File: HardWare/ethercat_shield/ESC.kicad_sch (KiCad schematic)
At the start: 39 parts, among them U8 AX58100-LQPF80, U9 BL24C16F-PARC, X1 25M

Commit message: Add test version
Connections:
- net GNDA is gone; now on net GND: C39.2, C40.2, C41.2, C42.2, C49.2
- net GNDD is gone; now on net GND: C35.2, C36.2, C37.2, C38.2, C43.2, C44.2, C45.2, C46.2, C47.2, C48.2

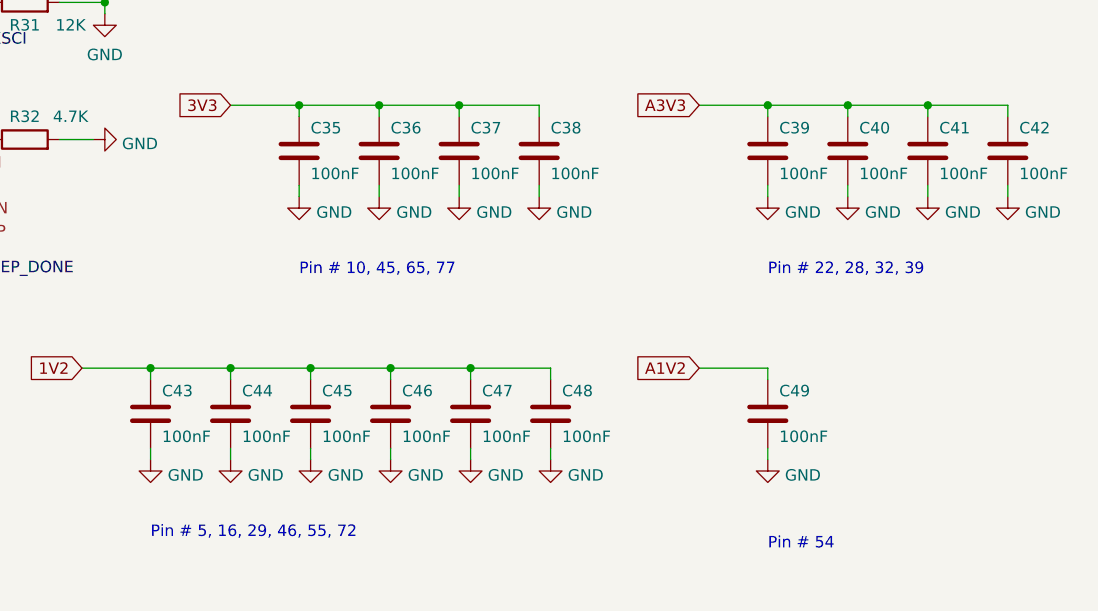
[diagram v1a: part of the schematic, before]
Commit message: 'ethercat_shield' PCB_layout completed
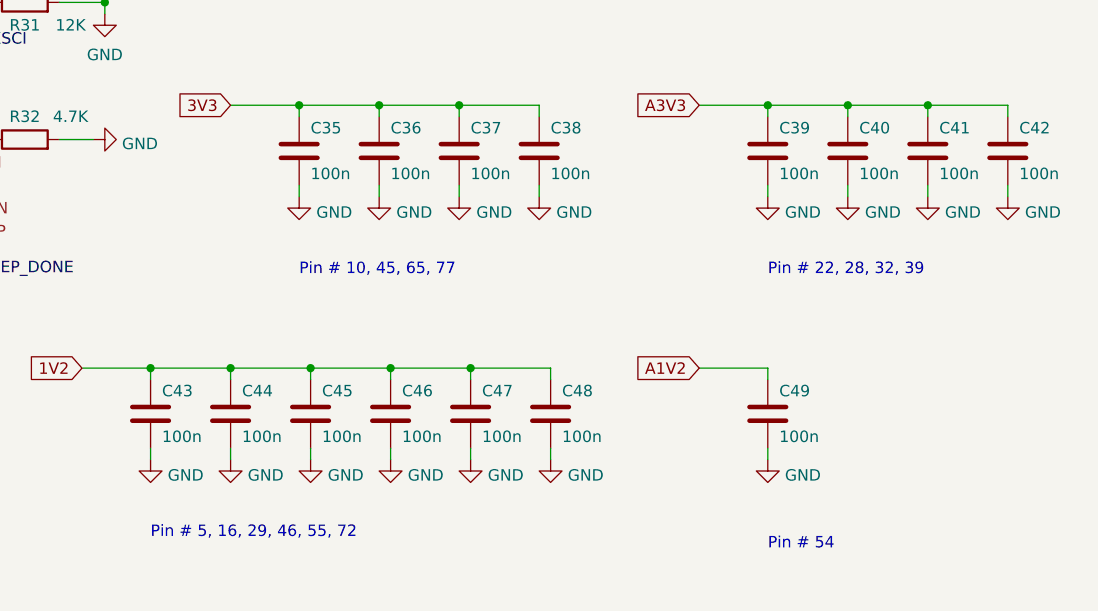
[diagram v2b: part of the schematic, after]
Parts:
- C35, C36, C37, C38, C39, C40, C41, C42, C43, C44, C45, C46, C47, C48, C49: value 100nF -> 100n
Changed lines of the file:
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@@
       (effects (font (size 1.27 1.27)) (justify left))
     )
-    (property "Value" "100nF" (id 1) (at 219.71 148.59 0)
+    (property "Value" "100n" (id 1) (at 219.71 148.59 0)
       (effects (font (size 1.27 1.27)) (justify left))
     )
@@
       (effects (font (size 1.27 1.27)) (justify left))
     )
-    (property "Value" "100nF" (id 1) (at 218.44 119.38 0)
+    (property "Value" "100n" (id 1) (at 218.44 119.38 0)
       (effects (font (size 1.27 1.27)) (justify left))
     )
@@
       (effects (font (size 1.27 1.27)) (justify left))
     )
-    (property "Value" "100nF" (id 1) (at 279.4 119.38 0)
+    (property "Value" "100n" (id 1) (at 279.4 119.38 0)
       (effects (font (size 1.27 1.27)) (justify left))
     )
@@
       (effects (font (size 1.27 1.27)) (justify left))
     )
-    (property "Value" "100nF" (id 1) (at 228.6 148.59 0)
+    (property "Value" "100n" (id 1) (at 228.6 148.59 0)
       (effects (font (size 1.27 1.27)) (justify left))
     )
@@
       (effects (font (size 1.27 1.27)) (justify left))
     )
-    (property "Value" "100nF" (id 1) (at 210.82 148.59 0)
+    (property "Value" "100n" (id 1) (at 210.82 148.59 0)
       (effects (font (size 1.27 1.27)) (justify left))
     )
@@
       (effects (font (size 1.27 1.27)) (justify left))
     )
-    (property "Value" "100nF" (id 1) (at 193.04 148.59 0)
+    (property "Value" "100n" (id 1) (at 193.04 148.59 0)
       (effects (font (size 1.27 1.27)) (justify left))
     )
@@
       (effects (font (size 1.27 1.27)) (justify left))
     )
-    (property "Value" "100nF" (id 1) (at 209.55 119.38 0)
+    (property "Value" "100n" (id 1) (at 209.55 119.38 0)
       (effects (font (size 1.27 1.27)) (justify left))
     )
@@
       (effects (font (size 1.27 1.27)) (justify left))
     )
-    (property "Value" "100nF" (id 1) (at 252.73 119.38 0)
+    (property "Value" "100n" (id 1) (at 252.73 119.38 0)
       (effects (font (size 1.27 1.27)) (justify left))
     )
@@
       (effects (font (size 1.27 1.27)) (justify left))
     )
-    (property "Value" "100nF" (id 1) (at 200.66 119.38 0)
+    (property "Value" "100n" (id 1) (at 200.66 119.38 0)
       (effects (font (size 1.27 1.27)) (justify left))
     )
@@
       (effects (font (size 1.27 1.27)) (justify left))
     )
-    (property "Value" "100nF" (id 1) (at 270.51 119.38 0)
+    (property "Value" "100n" (id 1) (at 270.51 119.38 0)
       (effects (font (size 1.27 1.27)) (justify left))
     )
@@
       (effects (font (size 1.27 1.27)) (justify left))
     )
-    (property "Value" "100nF" (id 1) (at 184.15 148.59 0)
+    (property "Value" "100n" (id 1) (at 184.15 148.59 0)
       (effects (font (size 1.27 1.27)) (justify left))
     )
@@
       (effects (font (size 1.27 1.27)) (justify left))
     )
-    (property "Value" "100nF" (id 1) (at 227.33 119.38 0)
+    (property "Value" "100n" (id 1) (at 227.33 119.38 0)
       (effects (font (size 1.27 1.27)) (justify left))
     )
@@
       (effects (font (size 1.27 1.27)) (justify left))
     )
-    (property "Value" "100nF" (id 1) (at 261.62 119.38 0)
+    (property "Value" "100n" (id 1) (at 261.62 119.38 0)
       (effects (font (size 1.27 1.27)) (justify left))
     )
@@
       (effects (font (size 1.27 1.27)) (justify left))
     )
-    (property "Value" "100nF" (id 1) (at 201.93 148.59 0)
+    (property "Value" "100n" (id 1) (at 201.93 148.59 0)
       (effects (font (size 1.27 1.27)) (justify left))
     )
@@
       (effects (font (size 1.27 1.27)) (justify left))
     )
-    (property "Value" "100nF" (id 1) (at 252.73 148.59 0)
-      (effects (font (size 1.27 1.27)) (justify left))
-    )
+    (property "Value" "100n" (id 1) (at 252.73 148.59 0)
+      (effects (font (size 1.27 1.27)) (justify left))
+    )
